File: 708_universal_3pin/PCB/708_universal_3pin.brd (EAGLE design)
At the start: 27.9 x 39.4 mm, 17 parts

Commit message: rename prod-number directory change breakout layout
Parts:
- removed J11, J12, J13, J14, J15: (no value), FaBo-etc:PIN_1X1_NONAME
- J1: device FaBo-Template:FABO_BRICK_SERIAL_UNIVERSAL -> FaBo-Template:FABO_BRICK_3PIN_UNIVERSAL
- moved J9 24.7 mm to (22.9, 15.2)
- moved J8 22.2 mm to (22.9, 12.7)
- moved J7 14.2 mm to (15.2, 12.7)
- moved J4 12.8 mm to (2.54, 12.7)
- moved J6 8.89 mm to (2.54, 25.4)
- moved J10 4.58 mm to (22.9, 25.4)
- moved J1 2.84 mm to (12.7, 16.5)
- moved J2 1.27 mm to (10.2, 12.7)
- moved J3 1.27 mm to (12.7, 12.7)
- moved U$3 1.27 mm to (12.7, 2.54)
- moved J5 1.27 mm to (2.54, 15.2)
- renumbered U$2 to U$1
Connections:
- removed net RX: J1.RX, J2.1
- removed net TX: J1.TX, J3.1
- new net IO: J1.IN/OUT, J2.1
- net GND: now also J7.1, J8.1, J9.1; no longer J11.1, J12.1, J13.1, J14.1, J15.1
- net VCC: now also J3.1; no longer J7.1, J8.1, J9.1
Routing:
- net VCC: track 35.1 -> 30.0 mm
- net TX: track 5.08 -> 0.00 mm
- net RX: track 5.08 -> 0.00 mm
- net IO: track 0.00 -> 5.08 mm
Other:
- board size 27.9 x 39.4 mm -> 25.4 x 33 mm
- board text added: "#708"
- board text added: "Rev.1.0.2"
- board text removed: "#702"
- board text removed: "Rev.1.0.1"

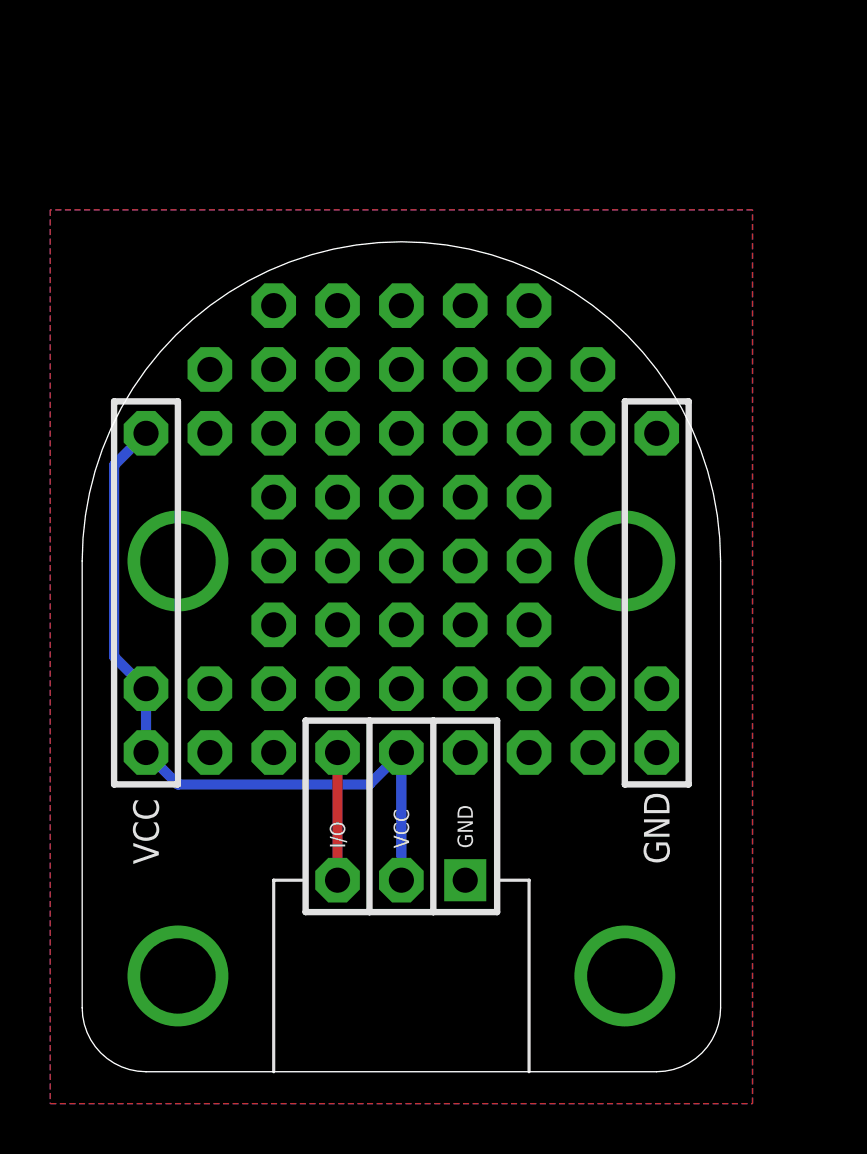
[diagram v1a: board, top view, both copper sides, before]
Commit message: fix solder land size
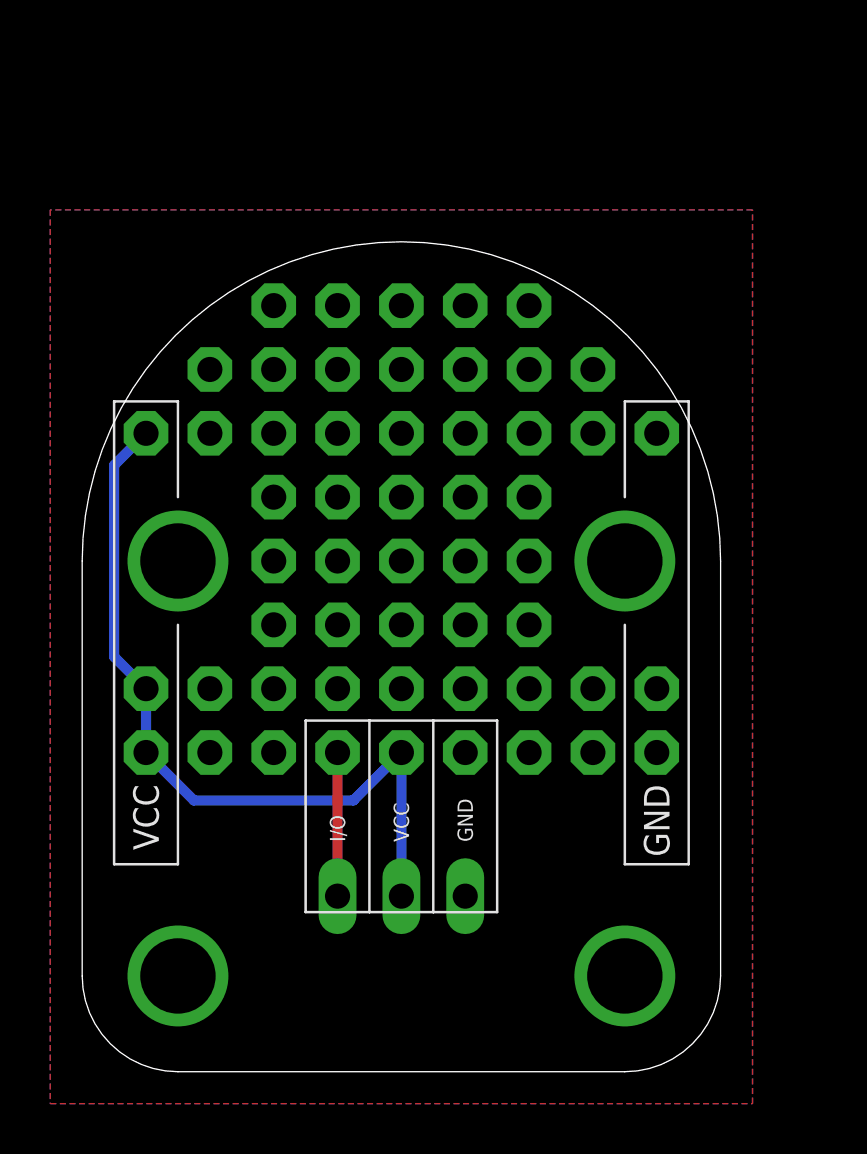
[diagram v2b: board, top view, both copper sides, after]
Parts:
- moved U$3 1.27 mm to (12.7, 1.27)
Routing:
- net VCC: track 30.0 -> 31.2 mm
- net IO: track 5.08 -> 5.71 mm
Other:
- outline, holes or cut-outs redrawn
- board text added: "Rev.1.0.3"
- board text removed: "Rev.1.0.2"
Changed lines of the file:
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@@
 <?xml version="1.0" encoding="utf-8"?>
 <!DOCTYPE eagle SYSTEM "eagle.dtd">
-<eagle version="7.4.0">
+<eagle version="7.5.0">
 <drawing>
 <settings>
@@
 <setting verticaltext="up"/>
 </settings>
-<grid distance="0.025" unitdist="inch" unit="inch" style="lines" multiple="1" display="yes" altdistance="0.025" altunitdist="inch" altunit="inch"/>
+<grid distance="25" unitdist="mil" unit="mil" style="lines" multiple="1" display="yes" altdistance="0.025" altunitdist="inch" altunit="inch"/>
 <layers>
 <layer number="1" name="Top" color="4" fill="1" visible="yes" active="yes"/>
@@
 <board>
 <plain>
-<wire x1="16.51" y1="6.35" x2="13.97" y2="6.35" width="0.254" layer="21"/>
-<wire x1="13.97" y1="6.35" x2="11.43" y2="6.35" width="0.254" layer="21"/>
-<wire x1="11.43" y1="6.35" x2="8.89" y2="6.35" width="0.254" layer="21"/>
-<wire x1="8.89" y1="6.35" x2="8.89" y2="13.97" width="0.254" layer="21"/>
-<wire x1="8.89" y1="13.97" x2="11.43" y2="13.97" width="0.254" layer="21"/>
-<wire x1="11.43" y1="13.97" x2="13.97" y2="13.97" width="0.254" layer="21"/>
-<wire x1="13.97" y1="13.97" x2="16.51" y2="13.97" width="0.254" layer="21"/>
-<wire x1="16.51" y1="13.97" x2="16.51" y2="6.35" width="0.254" layer="21"/>
-<wire x1="13.97" y1="13.97" x2="13.97" y2="6.35" width="0.254" layer="21"/>
-<wire x1="11.43" y1="13.97" x2="11.43" y2="6.35" width="0.254" layer="21"/>
-<wire x1="3.81" y1="26.67" x2="3.81" y2="11.43" width="0.254" layer="21"/>
-<wire x1="3.81" y1="11.43" x2="1.27" y2="11.43" width="0.254" layer="21"/>
-<wire x1="1.27" y1="11.43" x2="1.27" y2="26.67" width="0.254" layer="21"/>
-<wire x1="1.27" y1="26.67" x2="3.81" y2="26.67" width="0.254" layer="21"/>
-<wire x1="21.59" y1="26.67" x2="24.13" y2="26.67" width="0.254" layer="21"/>
-<wire x1="24.13" y1="26.67" x2="24.13" y2="11.43" width="0.254" layer="21"/>
-<wire x1="24.13" y1="11.43" x2="21.59" y2="11.43" width="0.254" layer="21"/>
-<wire x1="21.59" y1="11.43" x2="21.59" y2="26.67" width="0.254" layer="21"/>
-<text x="22.86" y="8.255" size="1.016" layer="21" font="vector" ratio="12" rot="R90" align="center-left">GND</text>
-<text x="2.54" y="8.255" size="1.016" layer="21" font="vector" ratio="12" rot="R90" align="center-left">VCC</text>
-<text x="12.7" y="2.54" size="0.8128" layer="22" font="vector" ratio="12" rot="MR180" align="bottom-center">MADE IN JAPAN</text>
-<text x="12.7" y="9.525" size="1.27" layer="22" font="vector" ratio="12" rot="MR0" align="bottom-center">Rev.1.0.2</text>
-<text x="21.59" y="8.255" size="1.778" layer="22" font="vector" ratio="12" rot="MR0" align="bottom-center">#708</text>
+<wire x1="16.51" y1="6.35" x2="13.97" y2="6.35" width="0.1" layer="21"/>
+<wire x1="13.97" y1="6.35" x2="11.43" y2="6.35" width="0.1" layer="21"/>
+<wire x1="11.43" y1="6.35" x2="8.89" y2="6.35" width="0.1" layer="21"/>
+<wire x1="8.89" y1="6.35" x2="8.89" y2="13.97" width="0.1" layer="21"/>
+<wire x1="8.89" y1="13.97" x2="11.43" y2="13.97" width="0.1" layer="21"/>
+<wire x1="11.43" y1="13.97" x2="13.97" y2="13.97" width="0.1" layer="21"/>
+<wire x1="13.97" y1="13.97" x2="16.51" y2="13.97" width="0.1" layer="21"/>
+<wire x1="16.51" y1="13.97" x2="16.51" y2="6.35" width="0.1" layer="21"/>
+<wire x1="13.97" y1="13.97" x2="13.97" y2="6.35" width="0.1" layer="21"/>
+<wire x1="11.43" y1="13.97" x2="11.43" y2="6.35" width="0.1" layer="21"/>
+<wire x1="3.81" y1="8.255" x2="1.27" y2="8.255" width="0.1" layer="21"/>
+<wire x1="1.27" y1="8.255" x2="1.27" y2="26.67" width="0.1" layer="21"/>
+<wire x1="1.27" y1="26.67" x2="3.81" y2="26.67" width="0.1" layer="21"/>
+<wire x1="21.59" y1="26.67" x2="24.13" y2="26.67" width="0.1" layer="21"/>
+<wire x1="24.13" y1="26.67" x2="24.13" y2="8.255" width="0.1" layer="21"/>
+<wire x1="24.13" y1="8.255" x2="21.59" y2="8.255" width="0.1" layer="21"/>
+<text x="22.86" y="11.43" size="1.016" layer="21" font="vector" ratio="12" rot="R270" align="center-left">GND</text>
+<text x="2.54" y="11.43" size="1.016" layer="21" font="vector" ratio="12" rot="R270" align="center-left">VCC</text>
+<text x="12.7" y="1.27" size="0.8128" layer="22" font="vector" ratio="12" rot="MR180" align="bottom-center">MADE IN JAPAN</text>
+<text x="12.7" y="9.525" size="1.27" layer="22" font="vector" ratio="12" rot="MR0" align="bottom-center">Rev.1.0.3</text>
+<text x="20.955" y="8.255" size="1.778" layer="22" font="vector" ratio="12" rot="MR0" align="bottom-center">#708</text>
+<wire x1="3.81" y1="22.86" x2="3.81" y2="26.67" width="0.1" layer="21"/>
+<wire x1="3.81" y1="8.255" x2="3.81" y2="17.78" width="0.1" layer="21"/>
+<wire x1="21.59" y1="22.86" x2="21.59" y2="26.67" width="0.1" layer="21"/>
+<wire x1="21.59" y1="8.255" x2="21.59" y2="17.78" width="0.1" layer="21"/>
 </plain>
 <attributes>
@@
 <element name="J10" library="FaBo-etc" package="PIN_1X1_NONAME" value="" x="22.86" y="25.4"/>
 <element name="U$1" library="FaBo-etc" package="LOGO_OSHW_S_BOTTOM" value="" x="3.81" y="8.89"/>
-<element name="U$3" library="FaBo-etc" package="LOGO_FABO_MS_BOTTOM" value="" x="12.7" y="2.54"/>
+<element name="U$3" library="FaBo-etc" package="LOGO_FABO_MS_BOTTOM" value="" x="12.7" y="1.27"/>
 </elements>
 <signals>
 <signal name="GND">
-<polygon width="0.4064" layer="1" spacing="0.254">
+<contactref element="J1" pad="GND"/>
+<contactref element="J7" pad="1"/>
+<contactref element="J8" pad="1"/>
+<contactref element="J9" pad="1"/>
+<contactref element="J10" pad="1"/>
+<polygon width="0.2032" layer="16" spacing="0.254">
 <vertex x="-1.27" y="-1.27"/>
 <vertex x="26.67" y="-1.27"/>
@@
 <vertex x="-1.27" y="34.29"/>
 </polygon>
-<polygon width="0.4064" layer="16" spacing="0.254">
+<polygon width="0.2032" layer="1" spacing="0.254">
 <vertex x="-1.27" y="-1.27"/>
 <vertex x="26.67" y="-1.27"/>
@@
 <vertex x="-1.27" y="34.29"/>
 </polygon>
-<contactref element="J1" pad="GND"/>
-<contactref element="J7" pad="1"/>
-<contactref element="J8" pad="1"/>
-<contactref element="J9" pad="1"/>
-<contactref element="J10" pad="1"/>
 </signal>
 <signal name="IO">
 <contactref element="J1" pad="IN/OUT"/>
 <contactref element="J2" pad="1"/>
-<wire x1="10.16" y1="12.7" x2="10.16" y2="7.62" width="0.4064" layer="1"/>
+<wire x1="10.16" y1="12.7" x2="10.16" y2="6.985" width="0.4064" layer="1"/>
 </signal>
 <signal name="VCC">
@@
 <contactref element="J5" pad="1"/>
 <contactref element="J6" pad="1"/>
-<wire x1="12.7" y1="7.62" x2="12.7" y2="12.7" width="0.4064" layer="16"/>
-<wire x1="12.7" y1="12.7" x2="11.43" y2="11.43" width="0.4064" layer="16"/>
-<wire x1="11.43" y1="11.43" x2="3.81" y2="11.43" width="0.4064" layer="16"/>
-<wire x1="3.81" y1="11.43" x2="2.54" y2="12.7" width="0.4064" layer="16"/>
-<wire x1="2.54" y1="12.7" x2="2.54" y2="15.24" width="0.4064" layer="16"/>
 <wire x1="2.54" y1="25.4" x2="1.27" y2="24.13" width="0.4064" layer="16"/>
 <wire x1="1.27" y1="24.13" x2="1.27" y2="16.51" width="0.4064" layer="16"/>
 <wire x1="1.27" y1="16.51" x2="2.54" y2="15.24" width="0.4064" layer="16"/>
+<wire x1="2.54" y1="15.24" x2="2.54" y2="12.7" width="0.4064" layer="16"/>
+<wire x1="2.54" y1="12.7" x2="4.445" y2="10.795" width="0.4064" layer="16"/>
+<wire x1="4.445" y1="10.795" x2="10.795" y2="10.795" width="0.4064" layer="16"/>
+<wire x1="10.795" y1="10.795" x2="12.7" y2="12.7" width="0.4064" layer="16"/>
+<wire x1="12.7" y1="6.985" x2="12.7" y2="12.7" width="0.4064" layer="16"/>
 </signal>
 </signals>

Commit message: change 708 jst connector
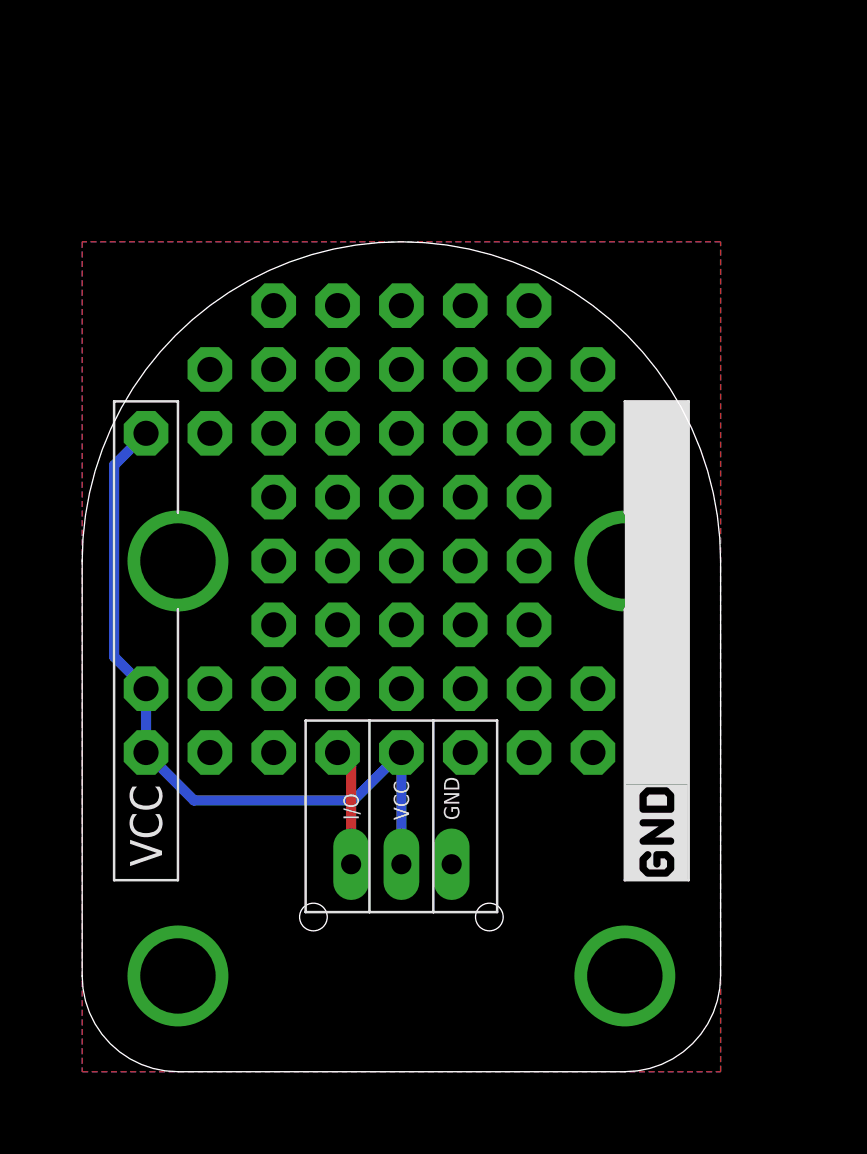
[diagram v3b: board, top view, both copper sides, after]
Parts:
- added U$4: (no value), FaBo-etc:LOGO_SILK_GND
- J10, J2, J3, J4, J5, J6, J7, J8, J9: device FaBo-etc:PIN_1X1_NONAME -> FaBo-PIN:PIN_1X1_NOLABEL
- U$1: device FaBo-etc:LOGO_OSHW_S_BOTTOM -> FaBo-etc:LOGO_OSHW_M_BOTTOM
- moved U$1 0.63 mm to (3.81, 8.26)
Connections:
- net IO: now also J1.I/O; no longer J1.IN/OUT
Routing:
- net VCC: track 31.2 -> 29.9 mm
- net IO: track 5.71 -> 4.67 mm
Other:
- board text added: "Rev.1.0.4"
- board text removed: "GND"
- board text removed: "Rev.1.0.3"

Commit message: fix gnd pattern
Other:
- board text added: "Rev.1.0.5"
- board text removed: "Rev.1.0.4"
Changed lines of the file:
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@@
 <text x="2.54" y="11.43" size="1.27" layer="21" font="vector" ratio="12" rot="R270" align="center-left">VCC</text>
 <text x="12.7" y="1.27" size="0.8128" layer="22" font="vector" ratio="12" rot="MR180" align="bottom-center">MADE IN JAPAN</text>
-<text x="21.59" y="7.62" size="1.016" layer="22" font="vector" ratio="12" rot="MR0" align="bottom-center">Rev.1.0.4</text>
+<text x="21.59" y="7.62" size="1.016" layer="22" font="vector" ratio="12" rot="MR0" align="bottom-center">Rev.1.0.5</text>
 <text x="21.59" y="8.89" size="1.9304" layer="22" font="vector" ratio="12" rot="MR0" align="bottom-center">#708</text>
 <wire x1="3.81" y1="22.225" x2="3.81" y2="26.67" width="0.1" layer="21"/>
@@
 <signal name="GND">
 <contactref element="J1" pad="GND"/>
-<polygon width="0.1524" layer="16" spacing="0.1524">
+<contactref element="J7" pad="1"/>
+<contactref element="J8" pad="1"/>
+<contactref element="J9" pad="1"/>
+<contactref element="J10" pad="1"/>
+<polygon width="0.2032" layer="16" spacing="0.2032">
 <vertex x="0" y="0"/>
 <vertex x="25.4" y="0"/>
@@
 <vertex x="0" y="33.02"/>
 </polygon>
-<polygon width="0.1524" layer="1" spacing="0.1524">
+<polygon width="0.2032" layer="1" spacing="0.2032">
 <vertex x="0" y="0"/>
 <vertex x="25.4" y="0"/>
@@
 <vertex x="0" y="33.02"/>
 </polygon>
-<contactref element="J7" pad="1"/>
-<contactref element="J8" pad="1"/>
-<contactref element="J9" pad="1"/>
-<contactref element="J10" pad="1"/>
 </signal>
 <signal name="IO">
